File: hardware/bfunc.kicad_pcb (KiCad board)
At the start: 2 copper layers, 46 parts, among them J1 Conn_02x03_Odd_Even, J10 Conn_01x20_Male, J2 Conn_01x02_Male, J3 Conn_Coaxial, J4 Conn_01x03_Male, J5 Conn_02x05_Odd_Even, J6 USB_B_Micro, J8 Conn_01x03_Male, J9 Conn_01x20_Male, SW1 SW_Push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

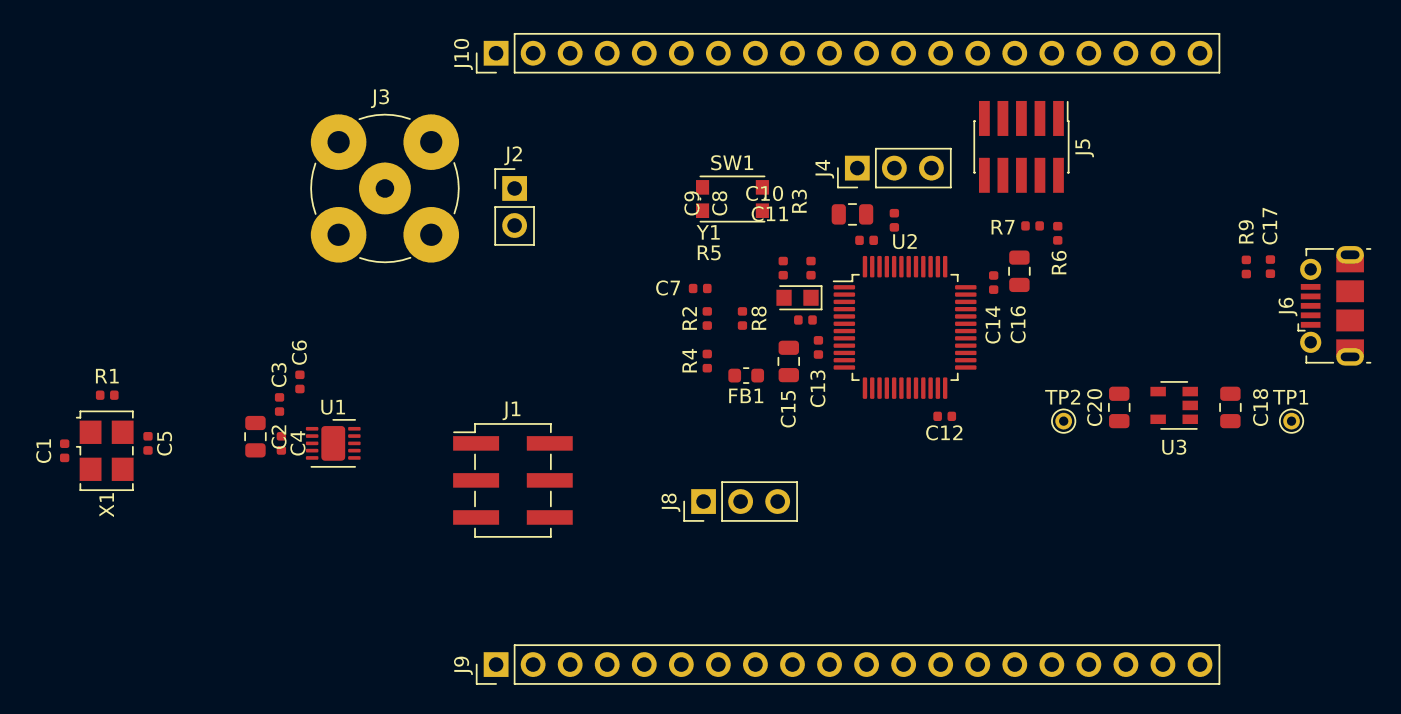
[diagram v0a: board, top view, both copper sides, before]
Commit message: Moved all Kicad stuff to /hardware/ directory
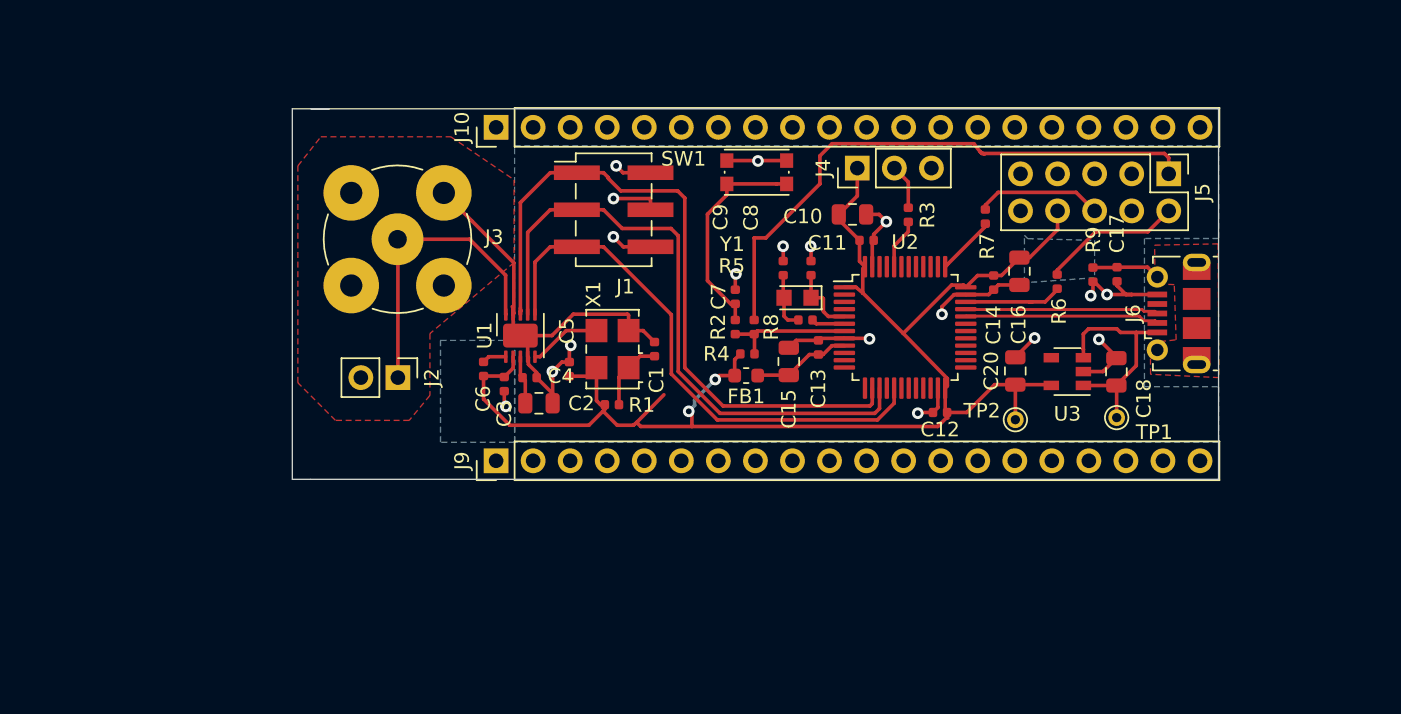
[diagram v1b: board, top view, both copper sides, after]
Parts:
- removed J8: Conn_01x03_Male, Connector_PinHeader_2.54mm:PinHeader_1x03_P2.54mm_Vertical
- J5: footprint Connector_PinHeader_1.27mm:PinHeader_2x05_P1.27mm_Vertical_SMD -> Connector_PinHeader_2.54mm:PinHeader_2x05_P2.54mm_Vertical
- moved C1 41.0 mm to (168.3, 76.2), turned to 90 degrees
- moved X1 35.4 mm to (165.5, 76.2), turned to 90 degrees
- moved R1 34.6 mm to (165.4, 80.0), turned to 0 degrees
- moved C5 29.3 mm to (162.5, 77.5), turned to 90 degrees
- moved J1 19.8 mm to (165.5, 66.6)
- moved C2 19.6 mm to (160.4, 79.9), turned to 0 degrees
- moved C4 17.6 mm to (159.8, 78.1), turned to 0 degrees
- moved C3 15.5 mm to (158.0, 78.6), turned to 270 degrees
- moved J2 15.2 mm to (150.7, 78.1), turned to 270 degrees
- moved U1 14.8 mm to (159.1, 75.2), turned to 90 degrees
- moved J9 14.0 mm to (157.5, 83.8)
- moved C6 12.6 mm to (156.6, 77.5)
- moved TP1 12.0 mm to (200.0, 80.9)
- moved C17 10.5 mm to (200.1, 71.0)
- moved J6 10.5 mm to (204.3, 73.7)
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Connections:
- net /MCU/USB_DM renamed /MCU/USB_D_N
- net /MCU/USB_DP renamed /MCU/USB_D_P
- C14 pad 1: (no net) -> +3V3
- J5 pad 1: +3V3 -> /MCU/RST_L_FLT
- J5 pad 10: /MCU/RST_L_FLT -> (no net)
- J5 pad 4: /MCU/SWCLK_FLT -> GND
- J5 pad 5: GND -> (no net)
- J5 pad 6: (no net) -> /MCU/SWCLK_FLT
- J5 pad 8: (no net) -> +3V3
- J5 pad 9: GND -> (no net)
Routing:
- net +3V3: track 0.00 -> 101.6 mm, vias 0 -> 2
- net GND: track 0.00 -> 85.5 mm, vias 0 -> 18
- net /DDS Chip/DDS_FSYNC: track 0.00 -> 47.5 mm
- net /DDS Chip/DDS_SCLK: track 0.00 -> 43.2 mm
- net /MCU/RST_L_FLT: track 0.00 -> 39.7 mm
- net /DDS Chip/DDS_SDATA: track 0.00 -> 37.5 mm
- net /DDS Chip/DDS_VOUT: track 0.00 -> 20.6 mm
- net +5V: track 0.00 -> 15.6 mm
- net Net-(C7-Pad1): track 0.00 -> 15.3 mm
- net /MCU/USB_D_N: track 0.00 -> 13.3 mm
- net /MCU/USB_D_P: track 0.00 -> 13.3 mm
- net /MCU/SWDIO_FLT: track 0.00 -> 9.63 mm
- net /MCU/RESET_L: track 0.00 -> 8.93 mm
- net /MCU/SWCLK_FLT: track 0.00 -> 8.68 mm
- net /MCU/SWDIO: track 0.00 -> 6.87 mm
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- added copper zone on B.Cu, net GND
- added copper zone on F.Cu, net GND
- added copper zone on F.Cu, net Net-(C17-Pad2)
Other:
- board outline added: 63.5 x 25.4 mm

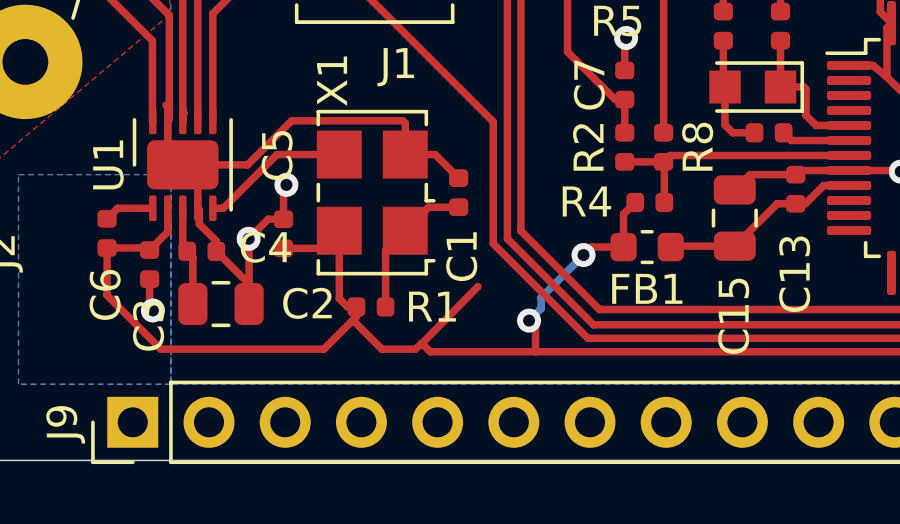
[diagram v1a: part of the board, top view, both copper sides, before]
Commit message: Minor updates on PCB reviewed for re-fab at CircuitHub
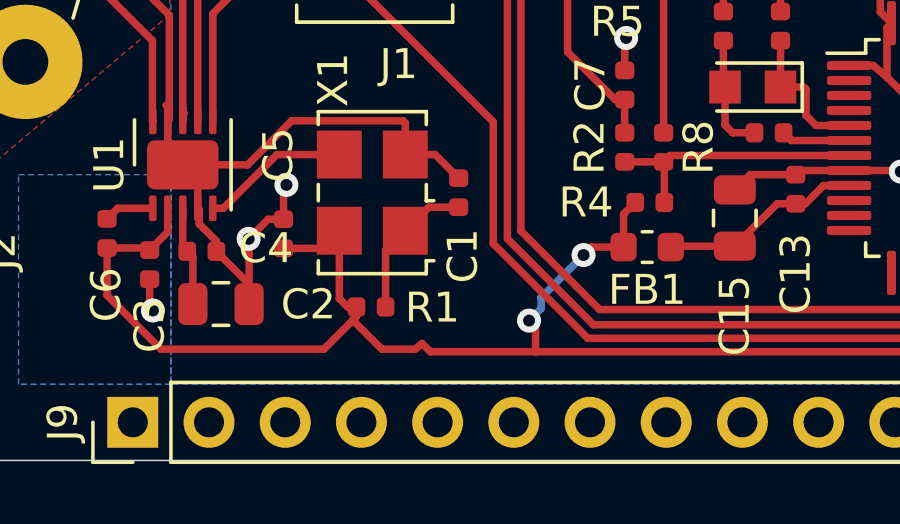
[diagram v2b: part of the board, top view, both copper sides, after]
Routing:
- net +3V3: track 101.6 -> 98.9 mm
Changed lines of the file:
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@@
     (thickness 1.6)
     (drawings 6)
-    (tracks 337)
+    (tracks 336)
     (zones 0)
     (modules 45)
@@
   (segment (start 188.40168 80.82784) (end 187.760702 81.468818) (width 0.25) (layer F.Cu) (net 4))
   (segment (start 188.40168 80.50784) (end 188.40168 80.82784) (width 0.25) (layer F.Cu) (net 4))
-  (segment (start 167.1193 81.1911) (end 168.98605 79.29387) (width 0.25) (layer F.Cu) (net 4))
   (segment (start 166.89832 81.3816) (end 167.1193 81.1911) (width 0.25) (layer F.Cu) (net 4))
   (segment (start 170.905582 81.468818) (end 170.905582 80.468882) (width 0.25) (layer F.Cu) (net 4))
